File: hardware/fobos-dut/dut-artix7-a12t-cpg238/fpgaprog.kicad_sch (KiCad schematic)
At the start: 13 parts

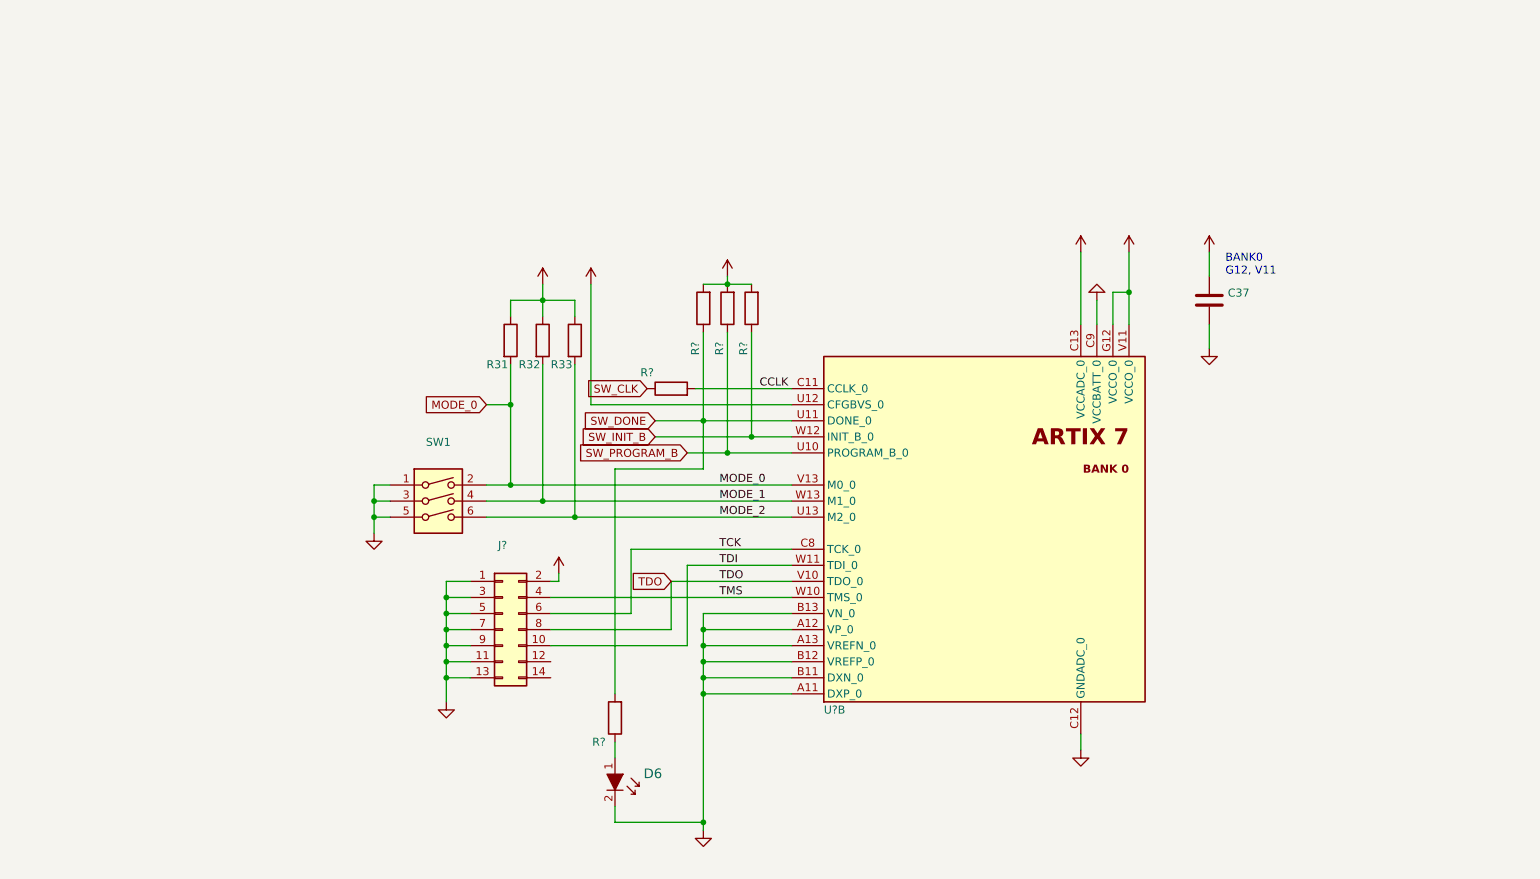
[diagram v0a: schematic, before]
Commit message: transitioned artix-7 dut to Kikad 6
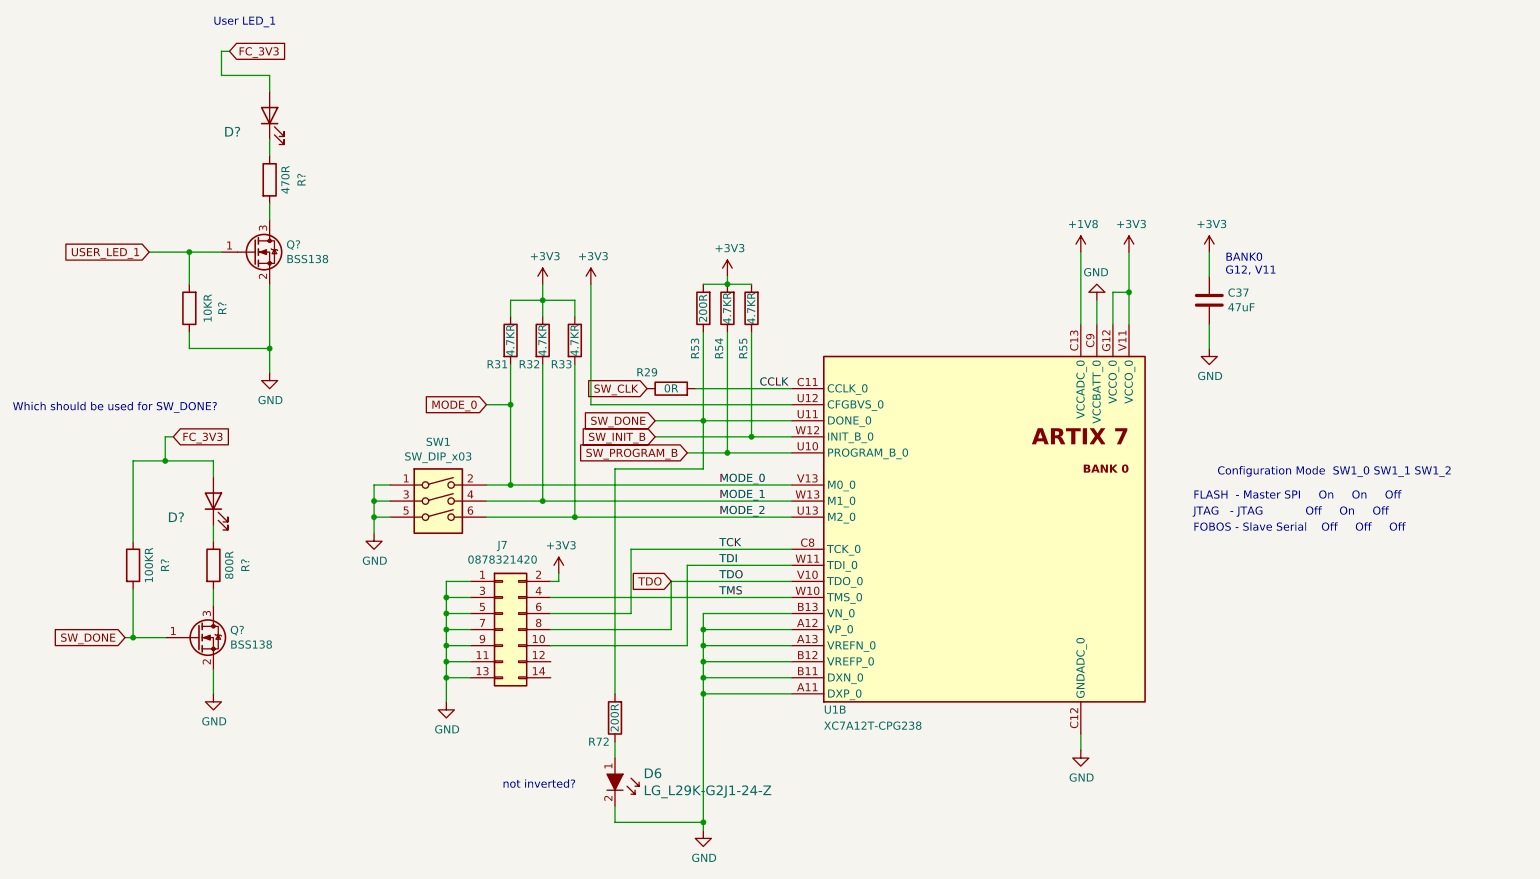
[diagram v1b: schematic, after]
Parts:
- added D? (x2): LG_L29K-G2J1-24-Z, LED_SMD:LED_0603_1608Metric, symbol Device:LED
- added Q? (x2): BSS138, Package_TO_SOT_SMD:SOT-23, symbol Transistor_FET:BSS138
- added R?: 10KR, Resistor_SMD:R_0603_1608Metric, symbol Device:R
- added R?: 800R, Resistor_SMD:R_0603_1608Metric, symbol Device:R
- added R?: 470R, Resistor_SMD:R_0603_1608Metric, symbol Device:R
- added R?: 100KR, Resistor_SMD:R_0603_1608Metric, symbol Device:R
- C37: value (none) -> 47uF; footprint (none) -> Capacitor_SMD:C_0603_1608Metric_Pad1.08x0.95mm_HandSolder
- D6: value (none) -> LG_L29K-G2J1-24-Z; footprint (none) -> LED_SMD:LED_0603_1608Metric
- J7: renamed from J?; value (none) -> 0878321420; footprint (none) -> cerg:PinHeader_2x7_P2mm_SMD
- R29: renamed from R?; value (none) -> 0R; footprint (none) -> Resistor_SMD:R_0603_1608Metric
- R31, R32, R33: value (none) -> 4.7KR; footprint (none) -> Resistor_SMD:R_0603_1608Metric
- R53, R72: renamed from R?; value (none) -> 200R; footprint (none) -> Resistor_SMD:R_0603_1608Metric
- R54, R55: renamed from R?; value (none) -> 4.7KR; footprint (none) -> Resistor_SMD:R_0603_1608Metric
- SW1: value (none) -> SW_DIP_x03; footprint (none) -> cerg:DS04-254-2-03BK-SMT
- U1: renamed from U?; value (none) -> XC7A12T-CPG238; footprint (none) -> Package_BGA:Xilinx_CPG238
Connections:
- net GND: now also Q?.2 (S), Q?.2 (S), R?.1
- net SW_DONE: now also Q?.1 (G), R?.2
- new net: D?.1 (K), R?.1 (x2)
- new net: Q?.3 (D), R?.2 (x2)
- new net FC_3V3: D?.2 (A), D?.2 (A), R?.1
- new net USER_LED_1: Q?.1 (G), R?.2
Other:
- note added: "Configuration Mode SW1_0 SW1_1 SW1_2"
- note added: "FLASH - Master SPI On On Off"
- note added: "FOBOS - Slave Serial Off Off Off"
- note added: "JTAG - JTAG Off On Off"
- note added: "User LED_1"
- note added: "Which should be used for SW_DONE?"
- note added: "not inverted?"
